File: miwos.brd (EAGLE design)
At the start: 120 x 120 mm, 50 parts

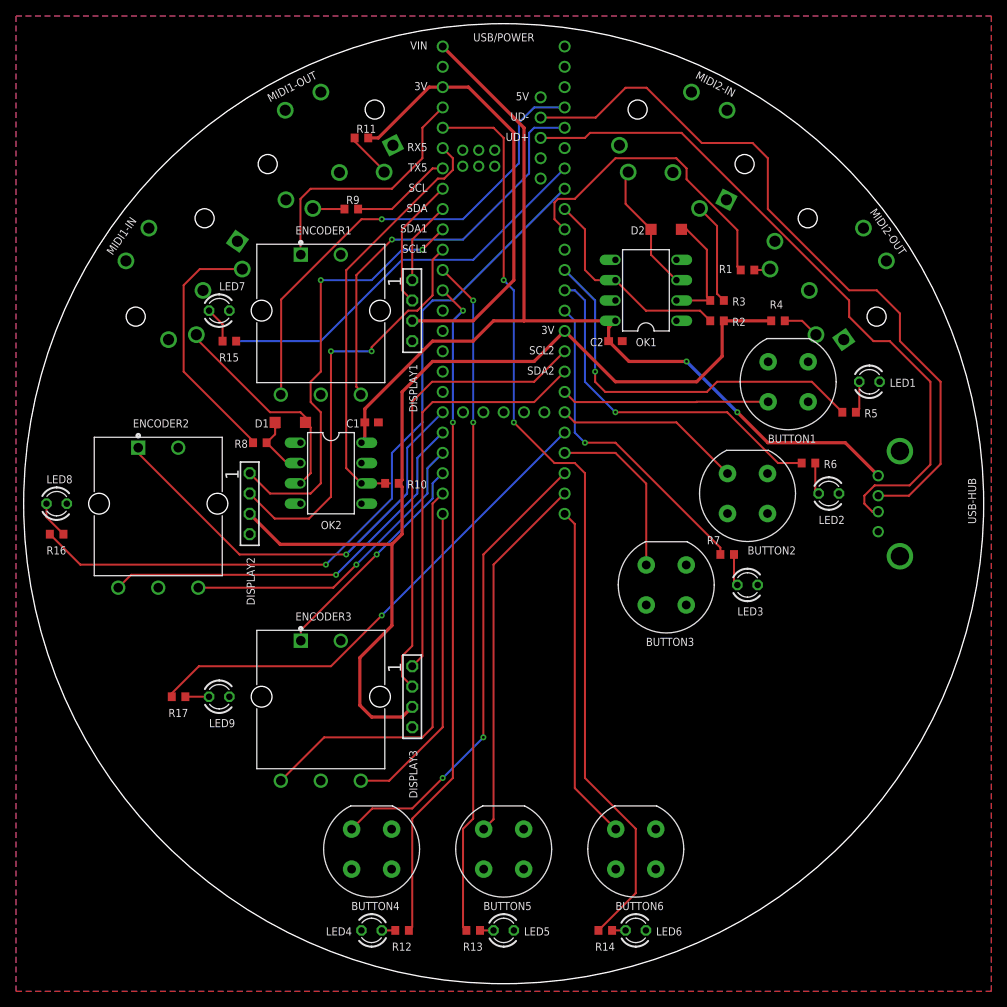
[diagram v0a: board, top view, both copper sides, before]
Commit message: Optimize ratsnest
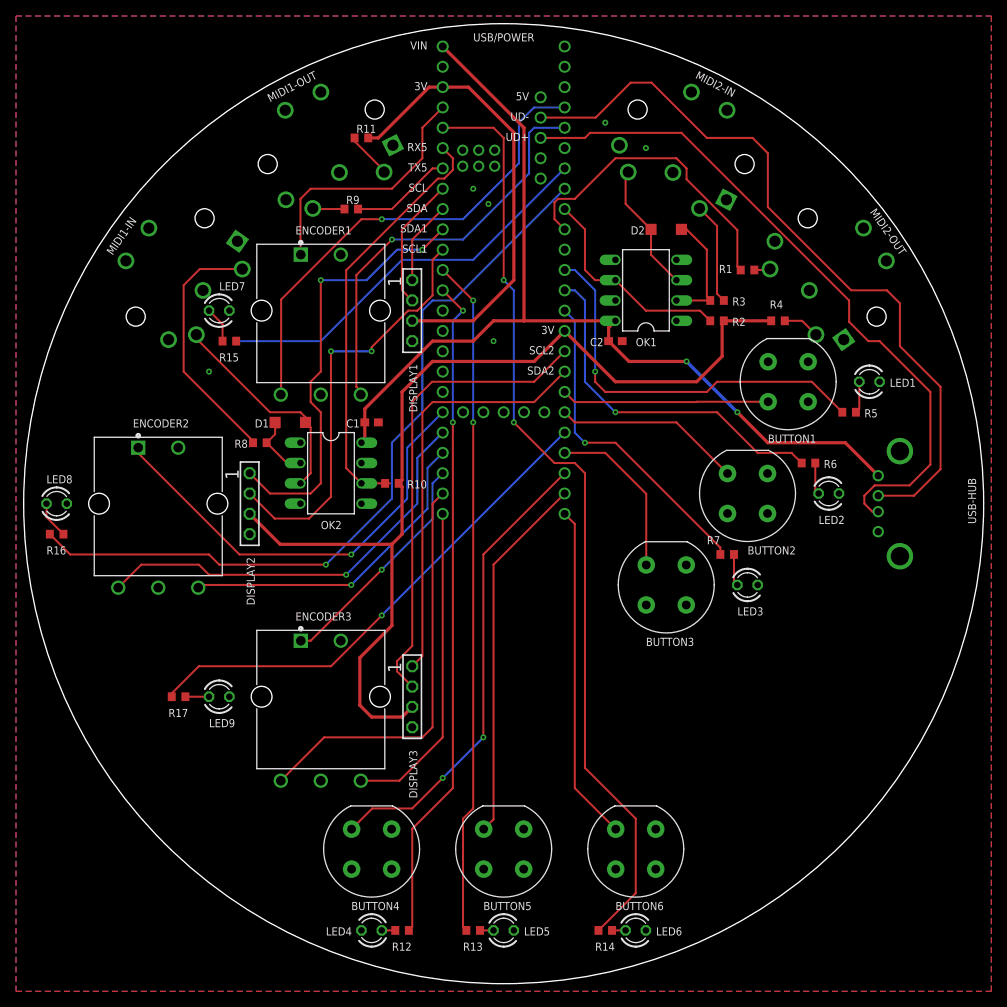
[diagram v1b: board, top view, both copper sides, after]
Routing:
- net N$2: track 92.2 -> 94.1 mm
- net ENCODER2-A: track 51.2 -> 53.0 mm
- net ENCODER2-B: track 39.4 -> 40.5 mm
- net ENCODER3-B: track 39.7 -> 40.4 mm
- net BUTTON3: track 22.0 -> 21.2 mm
- net BUTTON1-LED: track 49.1 -> 49.8 mm
- net ENCODER3-PUSH: track 28.3 -> 29.0 mm
- net SCL2: track 58.3 -> 58.8 mm

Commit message: Fix DRC errors
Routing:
- net BUTTON6: track 42.1 -> 47.1 mm
- net BUTTON5: track 46.1 -> 51.1 mm
- net BUTTON4: track 58.4 -> 63.4 mm
- net BUTTON3: track 21.2 -> 26.2 mm
- net BUTTON2: track 23.5 -> 28.5 mm
- net BUTTON1: track 26.0 -> 31.0 mm
- net ENCODER3-PUSH: track 29.0 -> 32.5 mm
- net ENCODER1-LED: track 49.6 -> 50.0 mm, vias 0 -> 1

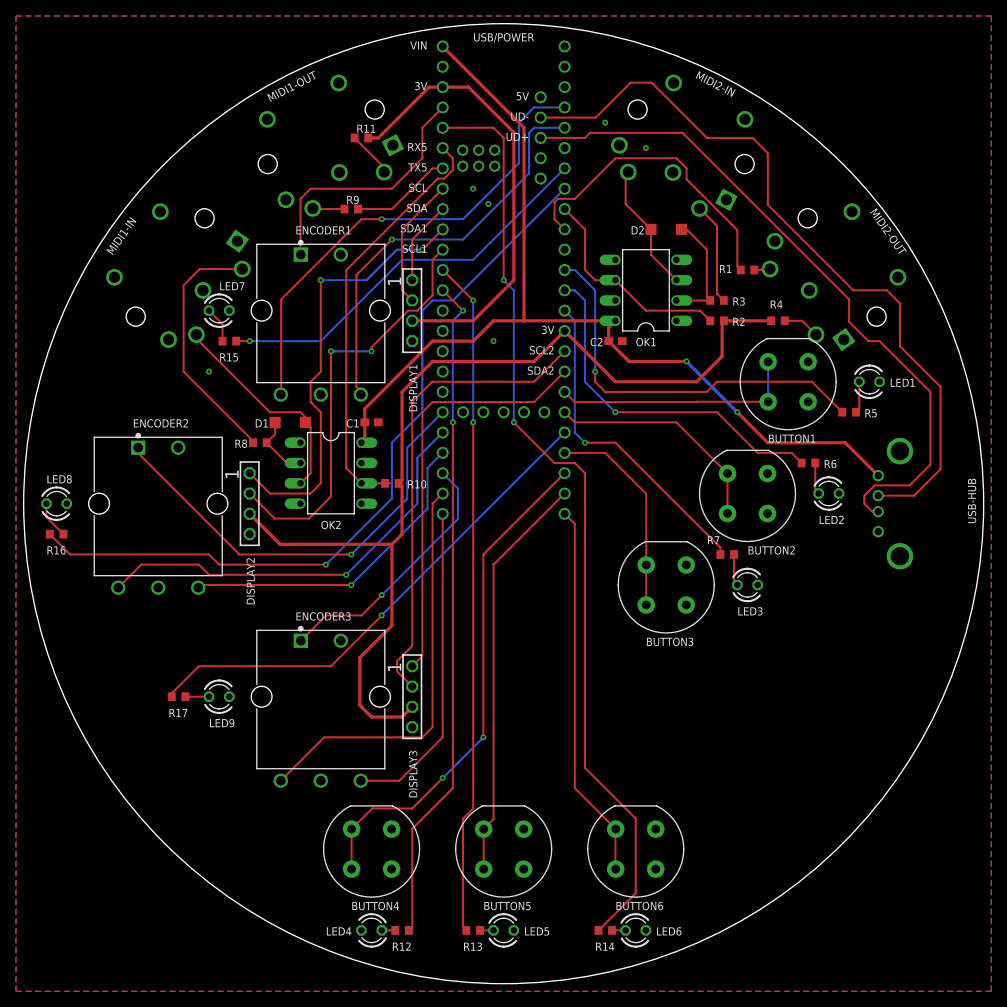
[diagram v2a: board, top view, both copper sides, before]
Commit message: Small fixes, add logo
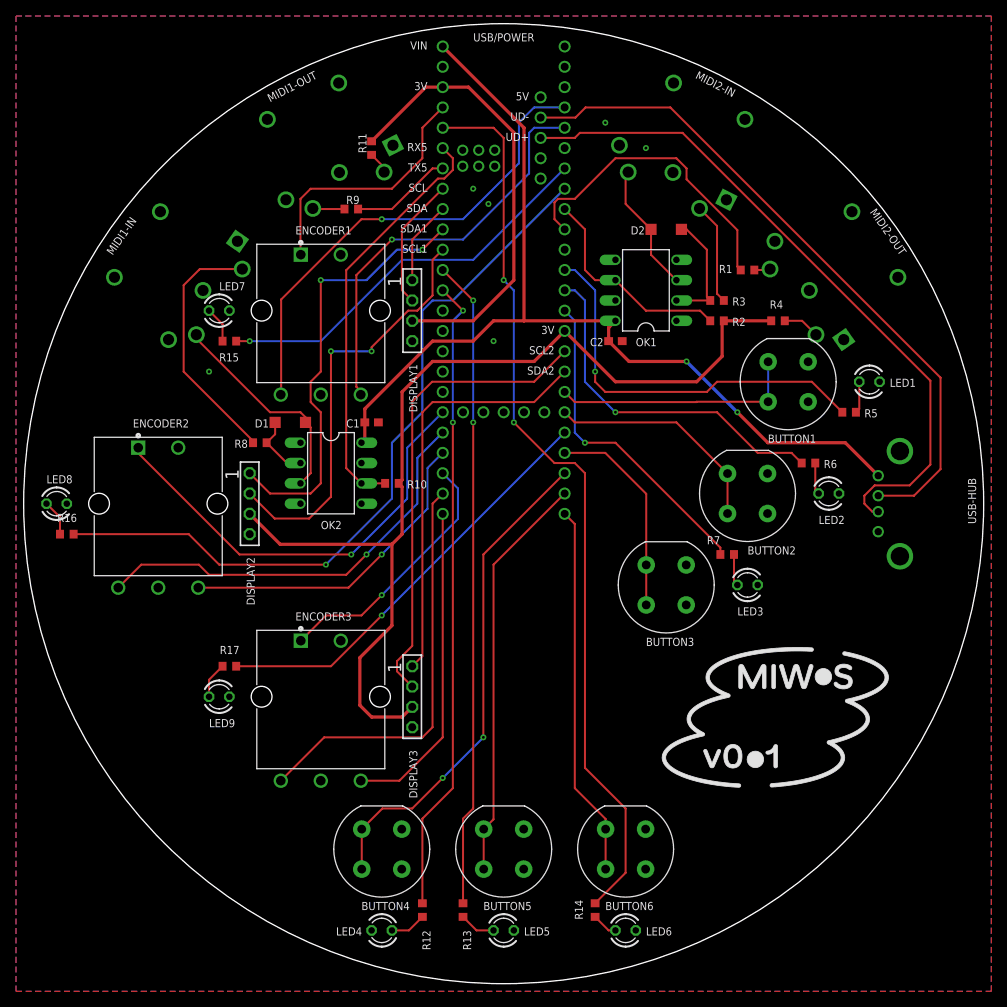
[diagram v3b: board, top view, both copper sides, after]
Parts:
- moved R17 7.41 mm to (-34.3, -20.3), turned to 180 degrees
- moved R12 3.59 mm to (-10.2, -50.8), turned to 270 degrees
- moved R13 2.84 mm to (-5.08, -50.8), turned to 270 degrees
- moved R14 2.84 mm to (11.4, -50.8), turned to 270 degrees
- moved R11 1.80 mm to (-16.5, 44.5), turned to 90 degrees
- moved R16 1.27 mm to (-54.6, -3.81), turned to 180 degrees
- moved BUTTON4 1.27 mm to (-15.2, -43.2)
- moved BUTTON6 1.27 mm to (15.2, -43.2)
- moved LED4 1.27 mm to (-15.2, -53.3)
- moved LED6 1.27 mm to (15.2, -53.3)
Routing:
- net ENCODER3-LED: track 63.0 -> 53.2 mm
- net N$2: track 93.9 -> 85.1 mm
- net BUTTON6-LED: track 117.5 -> 113.2 mm
- net BUTTON4-LED: track 83.9 -> 79.8 mm
- net BUTTON5-LED: track 84.8 -> 81.3 mm
- net N$12: track 5.80 -> 2.80 mm
- net ENCODER2-LED: track 96.9 -> 94.0 mm
- net N$13: track 1.69 -> 4.51 mm
- net N$14: track 1.82 -> 4.51 mm
- net N$15: track 1.69 -> 3.24 mm
- net N$22: track 2.96 -> 4.51 mm
- net BUTTON4: track 63.4 -> 62.2 mm
- net N$8: track 9.42 -> 8.26 mm
- net N$3: track 86.1 -> 85.3 mm
- net RX5: track 52.8 -> 52.2 mm
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
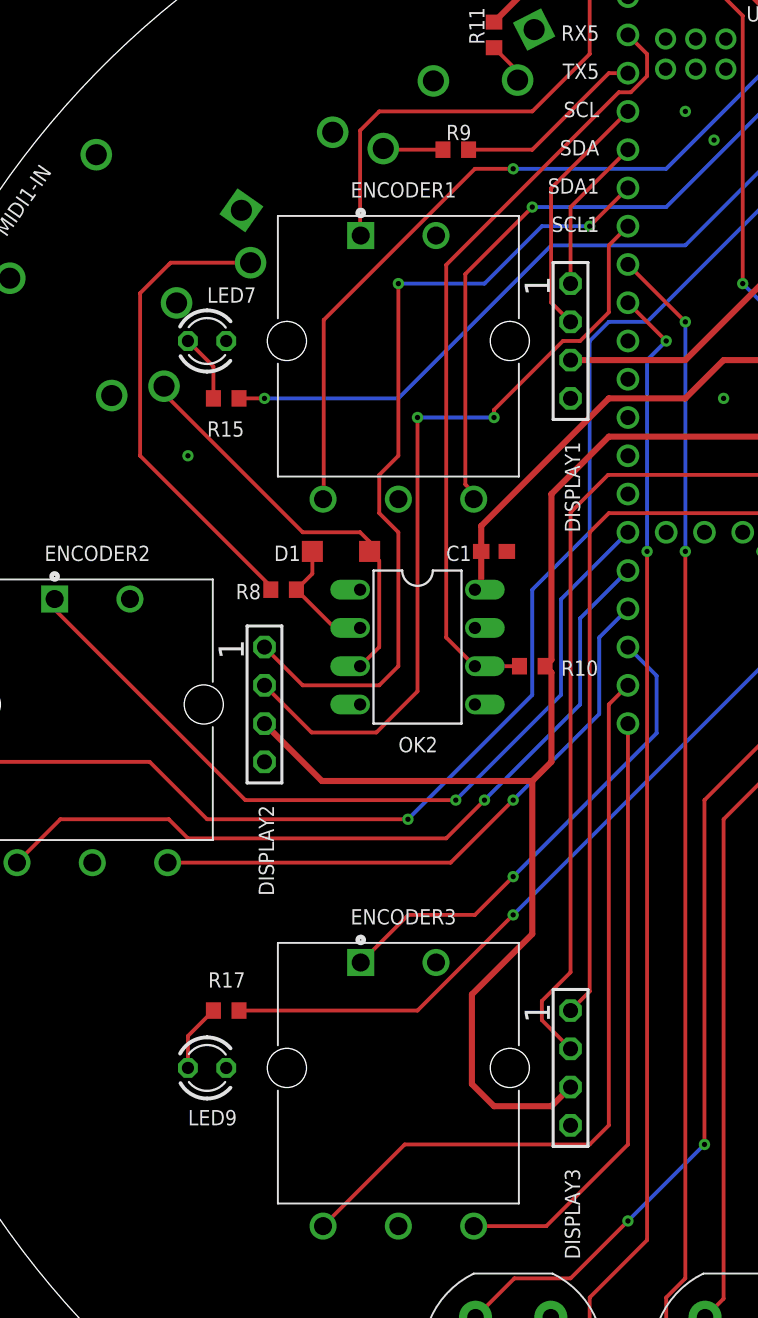
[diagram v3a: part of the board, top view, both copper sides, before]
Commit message: Fix wrong encoder wiring
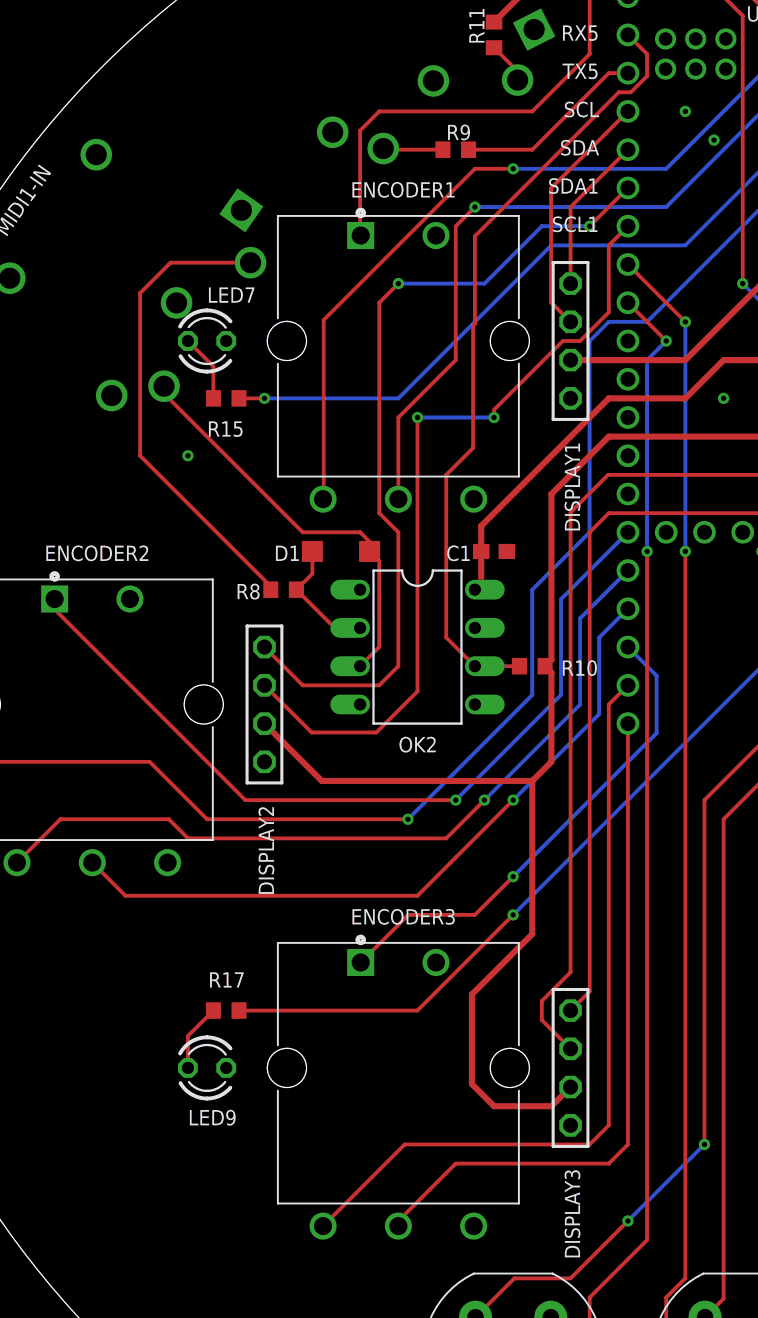
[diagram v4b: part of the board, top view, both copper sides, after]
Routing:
- net ENCODER2-B: track 40.5 -> 47.3 mm
- net ENCODER3-B: track 40.4 -> 45.6 mm
- net ENCODER1-B: track 51.8 -> 55.7 mm

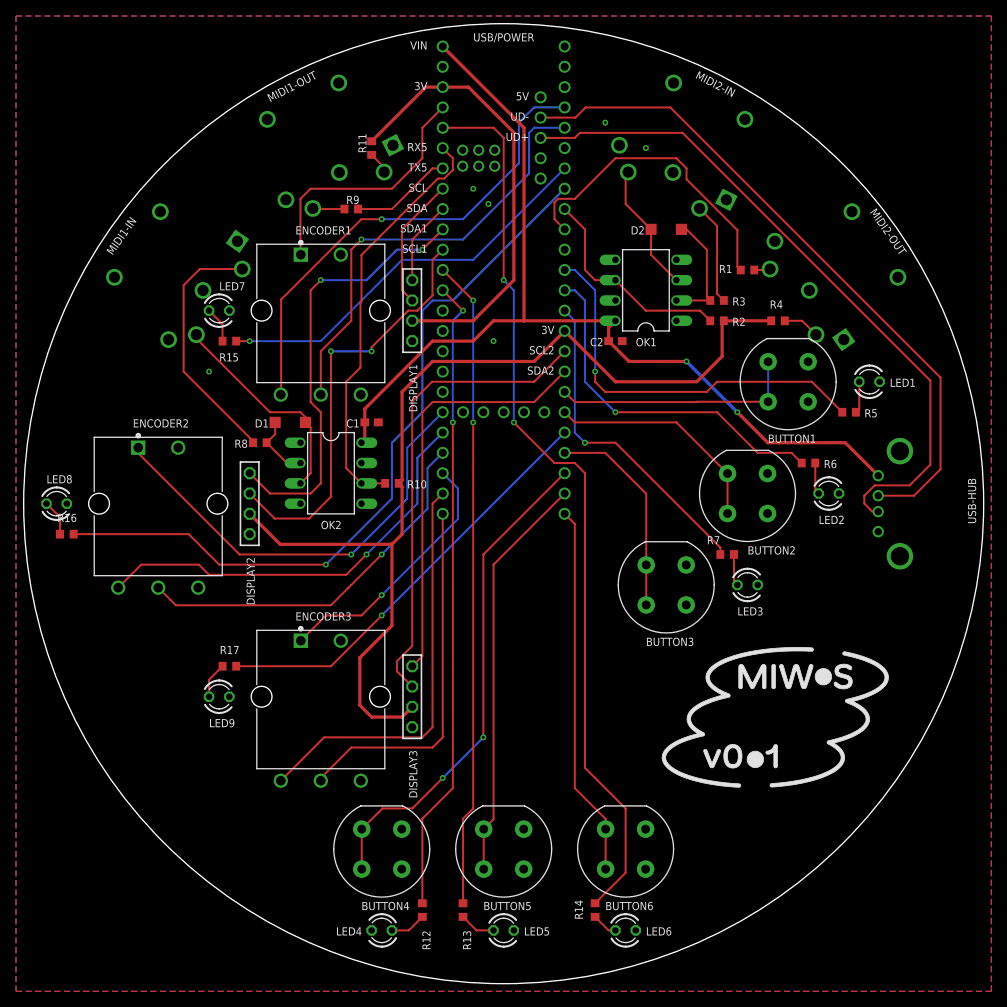
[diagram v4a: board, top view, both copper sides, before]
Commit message: Update to illuminated D6R buttons
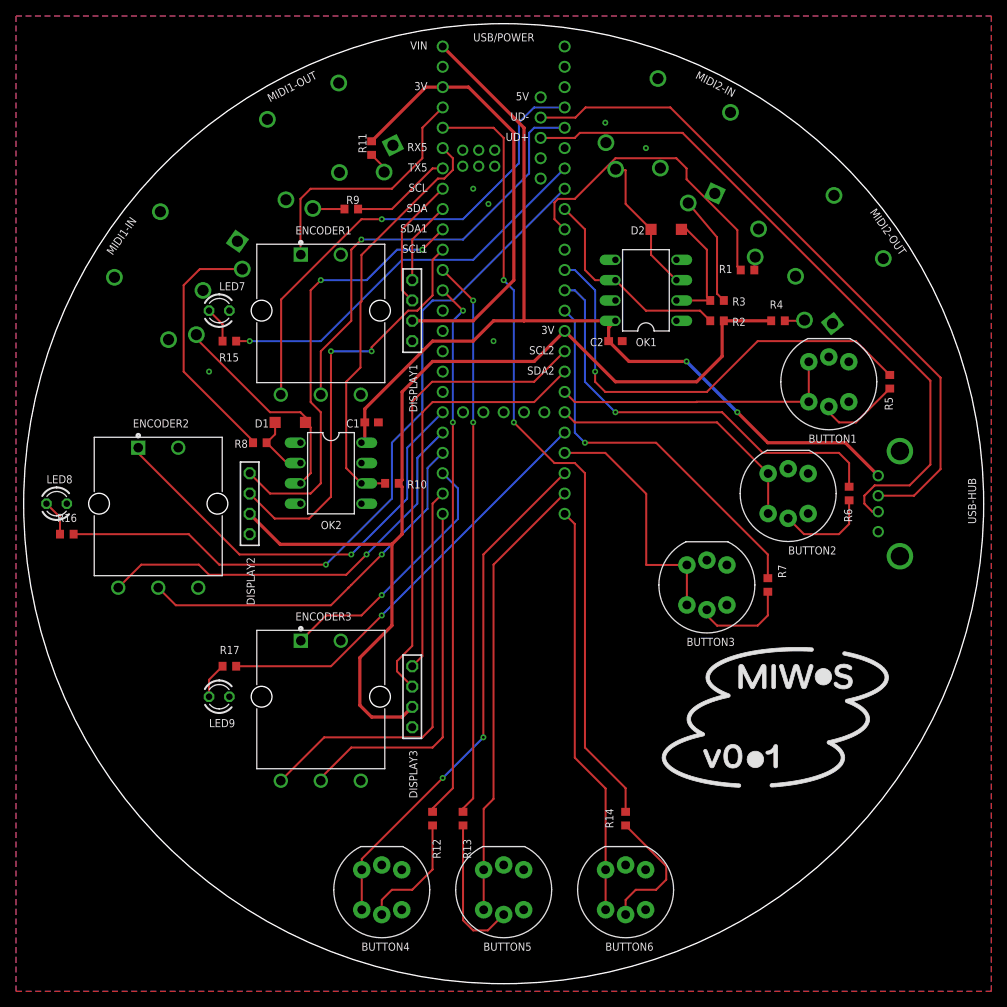
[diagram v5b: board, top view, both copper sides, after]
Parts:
- removed LED1, LED2, LED3, LED4, LED5, LED6: (no value), led:LED3MM
- BUTTON1, BUTTON2, BUTTON3, BUTTON4, BUTTON5, BUTTON6: value D6R90_F1_LFS -> D6RL; device D6R90_F1_LFS:SW_D6R90_F1_LFS -> D6RL:D6RL
- moved R14 12.0 mm to (15.2, -39.4)
- moved R12 11.5 mm to (-8.89, -39.4)
- moved R13 11.4 mm to (-5.08, -39.4)
- moved R7 6.35 mm to (33.0, -10.2), turned to 270 degrees
- moved R5 6.35 mm to (48.3, 15.2), turned to 270 degrees
- moved R6 6.35 mm to (43.2, 1.27), turned to 270 degrees
- moved BUTTON2 5.08 mm to (35.6, 1.27)
- moved BUTTON1 5.08 mm to (40.6, 15.2)
- moved BUTTON3 5.08 mm to (25.4, -10.2)
- moved BUTTON4 5.08 mm to (-15.2, -48.3)
- moved BUTTON5 5.08 mm to (0.00, -48.3)
- moved BUTTON6 5.08 mm to (15.2, -48.3)
- moved MIDI2-OUT 2.73 mm to (40.4, 31.5), turned to 322 degrees
- moved MIDI2-IN 1.84 mm to (21.7, 46.5), turned to 295 degrees
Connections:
- removed net N$7: LED3.A, R7.2
- new net N$23: BUTTON5.6, R13.2
- net GND: now also BUTTON1.5, BUTTON2.5, BUTTON3.5, BUTTON4.5, BUTTON5.5, BUTTON6.5; no longer LED1.K, LED2.K, LED3.K, LED4.K, LED5.K, LED6.K
- net N$13: now also BUTTON4.6; no longer LED4.A
- net N$14: now also BUTTON1.6, R5.2; no longer LED5.A, R13.2
- net N$15: now also BUTTON6.6; no longer LED6.A
- net N$5: now also BUTTON3.6, R7.2; no longer LED1.A, R5.2
- net N$6: now also BUTTON2.6; no longer LED2.A
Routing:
- net N$23: track 0.00 -> 18.3 mm
- net N$15: track 3.24 -> 16.8 mm
- net BUTTON6-LED: track 113.2 -> 100.2 mm
- net BUTTON4-LED: track 79.8 -> 67.8 mm
- net BUTTON5-LED: track 81.3 -> 69.8 mm
- net N$13: track 4.51 -> 15.3 mm
- net BUTTON2-LED: track 44.5 -> 53.4 mm
- net BUTTON3-LED: track 40.8 -> 49.2 mm
- net N$5: track 3.98 -> 12.3 mm
- net BUTTON1-LED: track 49.8 -> 58.0 mm
- net N$6: track 3.98 -> 11.9 mm
- net N$14: track 4.51 -> 10.6 mm
- net BUTTON1: track 31.0 -> 36.1 mm
- net BUTTON2: track 28.5 -> 33.6 mm
- net BUTTON6: track 46.5 -> 51.6 mm
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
